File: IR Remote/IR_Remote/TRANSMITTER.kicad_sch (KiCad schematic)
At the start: 0 parts

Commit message: Task 01, pcb done
dont forget about gitignore
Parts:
- added BT?: 9V_Batt, symbol Device:Battery
- added C?: 220uF, Capacitor_Tantalum_SMD:CP_EIA-3216-18_Kemet-A_Pad1.58x1.35mm_HandSolder, symbol Device:C_Polarized
- added C?: 220nF, Capacitor_SMD:C_0805_2012Metric_Pad1.18x1.45mm_HandSolder, symbol Device:C
- added R?: 47R, Resistor_SMD:R_0805_2012Metric_Pad1.20x1.40mm_HandSolder, symbol Device:R
- added SW?: SW_Push, symbol Switch:SW_Push
- added U?: NA555D, Package_SO:SOIC-8_3.9x4.9mm_P1.27mm, symbol Timer:NA555D
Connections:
- new net: C?.1, C?.2, R?.2, SW?.1
- new net: BT?.1 (+), R?.1
- new net +9V: SW?.2
- new net GND: BT?.2 (-), C?.1, C?.2
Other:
- title: (none) -> IR Remote

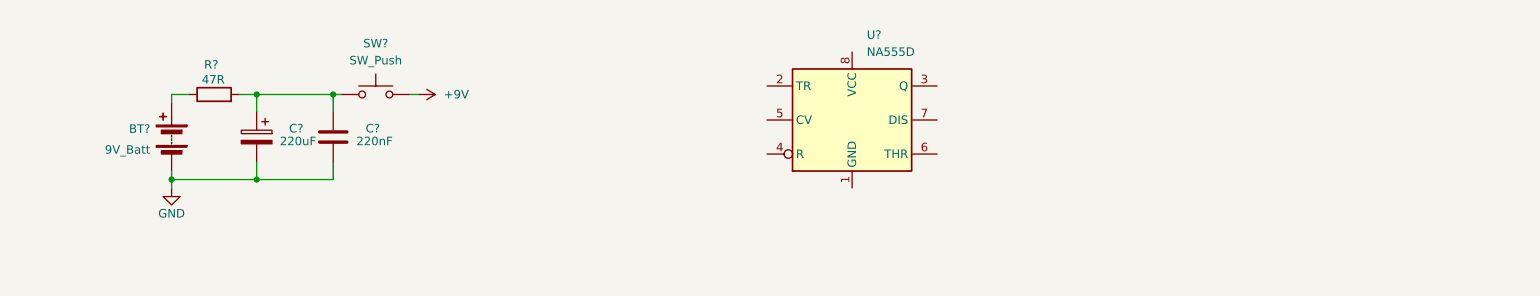
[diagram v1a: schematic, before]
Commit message: Knops IR emitter schematic
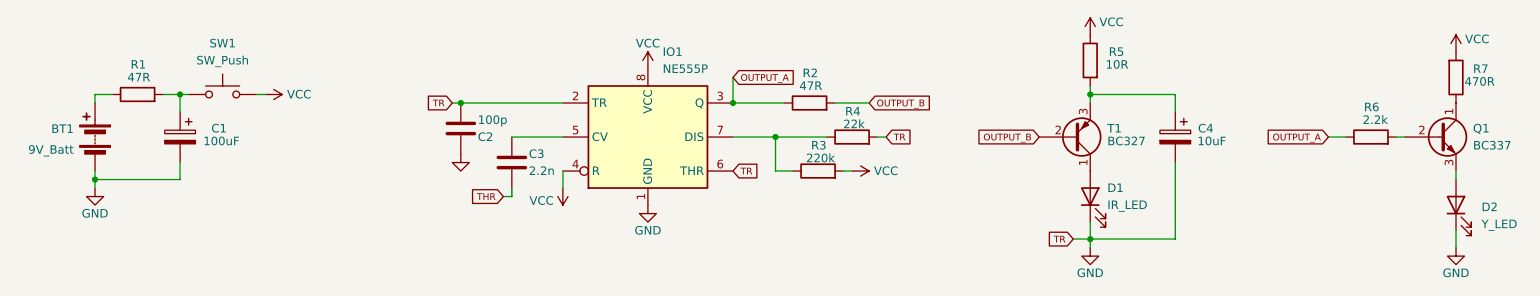
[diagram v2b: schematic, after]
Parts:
- removed C?: 220nF, Capacitor_SMD:C_0805_2012Metric_Pad1.18x1.45mm_HandSolder, symbol Device:C
- removed U?: NA555D, Package_SO:SOIC-8_3.9x4.9mm_P1.27mm, symbol Timer:NA555D
- added C2: 100p, symbol Device:C
- added C3: 2.2n, symbol Device:C
- added C4: 10uF, Capacitor_Tantalum_SMD:CP_EIA-3216-18_Kemet-A_Pad1.58x1.35mm_HandSolder, symbol Device:C_Polarized
- added D1: IR_LED, symbol Device:LED
- added D2: Y_LED, symbol Device:LED
- added IO1: NE555P, Package_DIP:DIP-8_W7.62mm, symbol Timer:NE555P
- added Q1: BC337, Package_TO_SOT_THT:TO-92_Inline, symbol Transistor_BJT:BC337
- added R2: 47R, Resistor_SMD:R_0805_2012Metric_Pad1.20x1.40mm_HandSolder, symbol Device:R
- added R3: 220k, Resistor_SMD:R_0805_2012Metric_Pad1.20x1.40mm_HandSolder, symbol Device:R
- added R4: 22k, Resistor_SMD:R_0805_2012Metric_Pad1.20x1.40mm_HandSolder, symbol Device:R
- added R5: 10R, Resistor_SMD:R_0805_2012Metric_Pad1.20x1.40mm_HandSolder, symbol Device:R
- added R6: 2.2k, Resistor_SMD:R_0805_2012Metric_Pad1.20x1.40mm_HandSolder, symbol Device:R
- added R7: 470R, Resistor_SMD:R_0805_2012Metric_Pad1.20x1.40mm_HandSolder, symbol Device:R
- added T1: BC327, Package_TO_SOT_THT:TO-92_Inline, symbol Transistor_BJT:BC327
- C1: renamed from C?; value 220uF -> 100uF
- gave numbers to parts that had none: 3
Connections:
- net GND: now also C2.1, C2.2, C4.2, D1.1 (K), D2.1 (K), IO1.1 (GND), IO1.2 (TR), IO1.6 (THR), R4.2
- net +9V renamed VCC
- net VCC: now also IO1.4 (R), IO1.8 (VCC), R3.2, R5.1, R7.2
- new net: C3.1, IO1.5 (CV)
- new net: IO1.7 (DIS), R3.1, R4.1
- new net: D1.2 (A), T1.1 (C)
- new net: C4.1, R5.2, T1.3 (E)
- new net: Q1.1 (C), R7.1
- new net: Q1.2 (B), R6.2
- new net: D2.2 (A), Q1.3 (E)
- new net OUTPUT_A: IO1.3 (Q), R2.1, R6.1
- new net OUTPUT_B: R2.2, T1.2 (B)
- new net THR: C3.2
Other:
- moved on the sheet: BT1, C1, R1, SW1
